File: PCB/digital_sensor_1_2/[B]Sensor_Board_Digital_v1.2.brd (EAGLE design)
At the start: 45 x 30 mm, 15 parts, among them J1 RJ11REVERSE, J2 RJ45_MX-95001-2881, U2 CC2D23-CHIPCAP2, U3 MS5637-02BA03

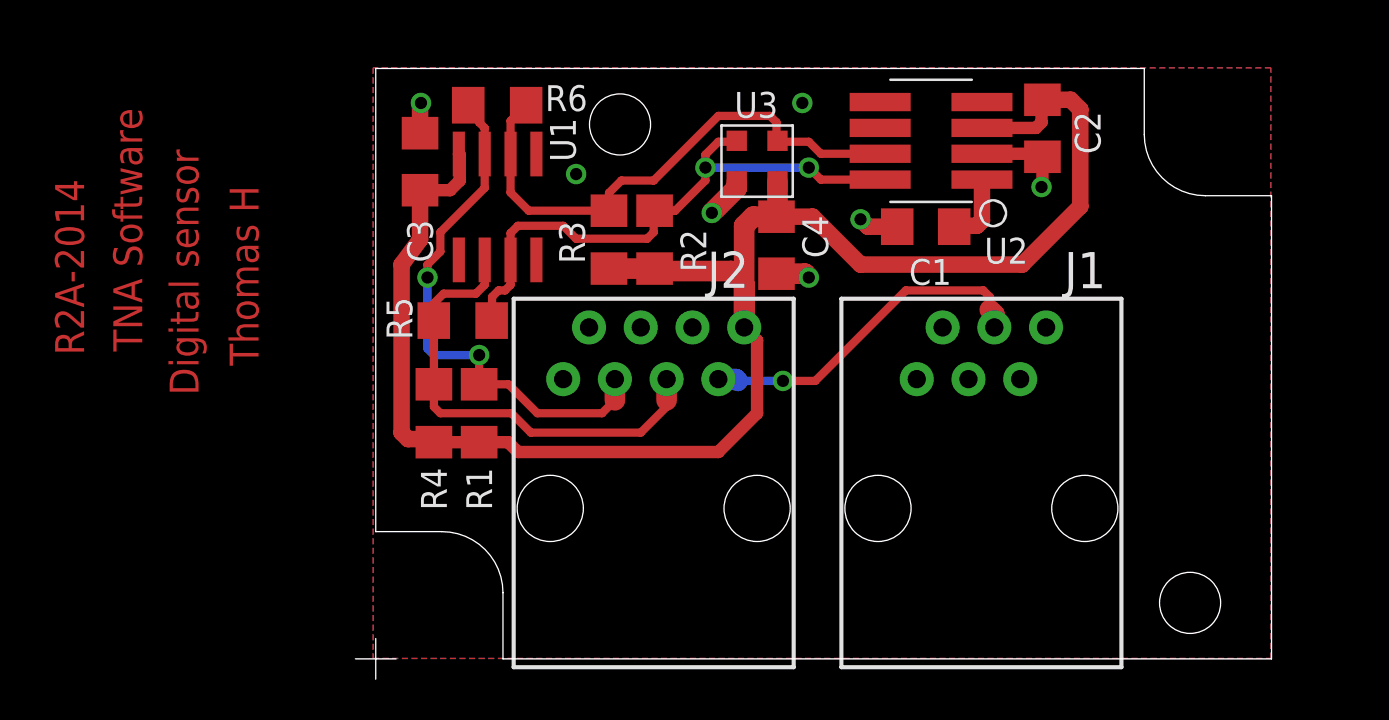
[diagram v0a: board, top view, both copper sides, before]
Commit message: Latest revision of PCB with support for RainGauge and some other sensors.
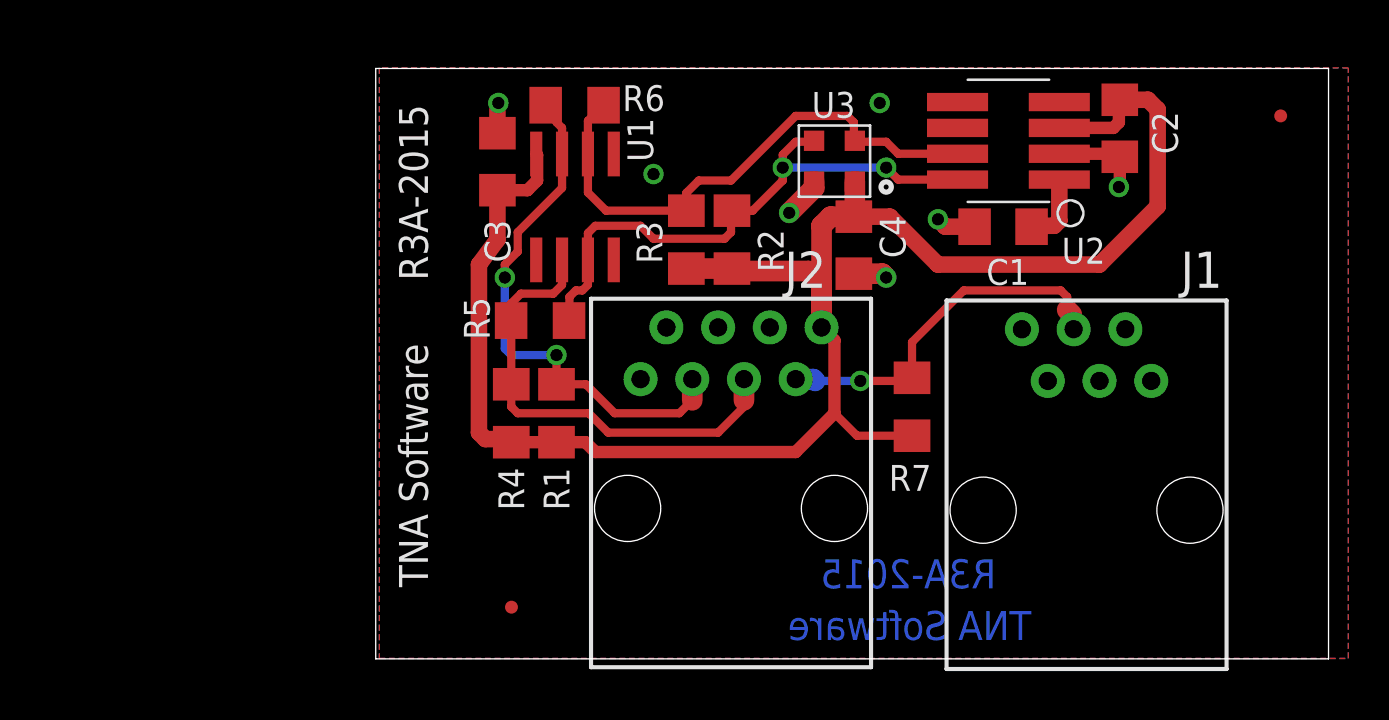
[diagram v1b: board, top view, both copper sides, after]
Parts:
- added JP1, JP2: FIDUCIALUFIDUCIAL, SparkFun:MICRO-FIDUCIAL
- added R7: 4k7, rcl:R1206
- J1: value RJ11REVERSE -> RJ12MX-95001-2661; device Thomas Egnal Library:MX-95001-2661@1 -> Thomas Egnal Library:MX-95001-2661
- moved J1 5.17 mm to (34.9, 7.30)
- moved C1 3.80 mm to (30.8, 21.2)
- moved C4 3.80 mm to (23.5, 20.3)
- moved J2 3.80 mm to (17.5, 7.39)
- moved R1 3.80 mm to (8.88, 12.1)
- moved R3 3.80 mm to (15.3, 20.6)
- moved R6 3.80 mm to (9.77, 27.2)
- moved U2 3.80 mm to (31.1, 25.4)
- moved C3 3.80 mm to (5.98, 24.4)
- moved R4 3.80 mm to (6.66, 12.1)
- moved R5 3.80 mm to (8.07, 16.6)
- moved U1 3.80 mm to (9.79, 22.2)
- moved R2 3.80 mm to (17.5, 20.6)
- moved C2 3.80 mm to (36.5, 26.1)
- moved U3 3.80 mm to (22.5, 24.4)
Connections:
- net +3V3: now also R7.1
- net GND: now also J1.4; no longer J1.3
- net RAINSENSOR: now also J1.3, R7.2; no longer J1.4
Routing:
- net +3V3: track 84.4 -> 88.7 mm
- net RAINSENSOR: track 16.9 -> 18.1 mm
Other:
- board size 45 x 30 mm -> 46.8 x 29 mm
- board text added: "R3A-2015"
- board text removed: "Digital sensor"
- board text removed: "R2A-2014"
- board text removed: "Thomas H"
